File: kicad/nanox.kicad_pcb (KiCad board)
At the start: 4 copper layers, 61.7 x 15.9 mm, 142 parts, among them P1 likely an ESD protection diod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, P2 likely an ESD protection diod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, P3 likely an ESD protection diod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, P4 likely an ESD protection diod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, P5 likely an ESD protection diod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, SW1 push button, left, SW2 push button, right, X1 ?, X10 TI TLV61046A boost converter 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, X11 unknown, marked AF, likely a 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, X12 unknown, likely a P-channel M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, X2 likely an N-channel MOSFET: t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, X3 likely an N-channel MOSFET: t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, X4 ?, X5 ?, X6 ?, X7 ?, X8 ?, X9 NXP PMBZ5246B 16 V Zener diod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, Y1 32 MHz crystal (HSE), Y2 not populated: 32.768 kHz cry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

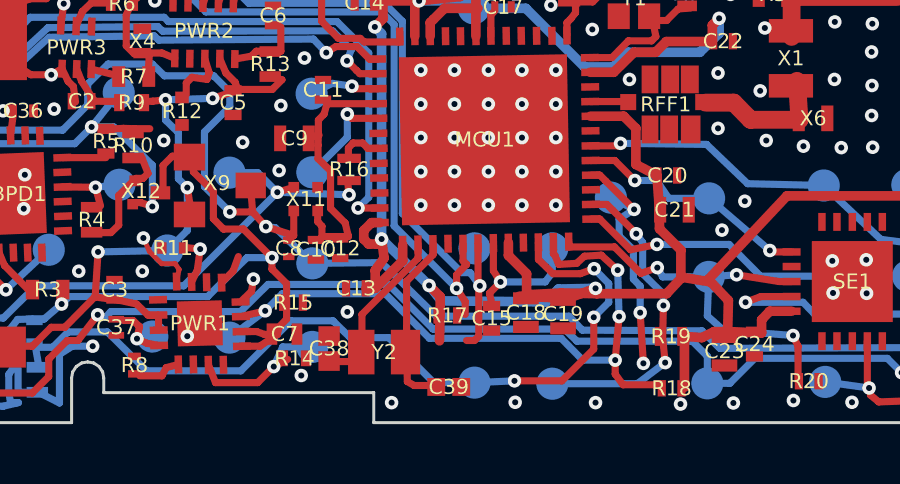
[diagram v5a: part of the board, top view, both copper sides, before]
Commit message: Move R17 onto the I2C1 SCL trace: the clock's pull-up to +3.3V
Co-Authored-By: Claude Opus 5.5 <noreply@anthropic.com>
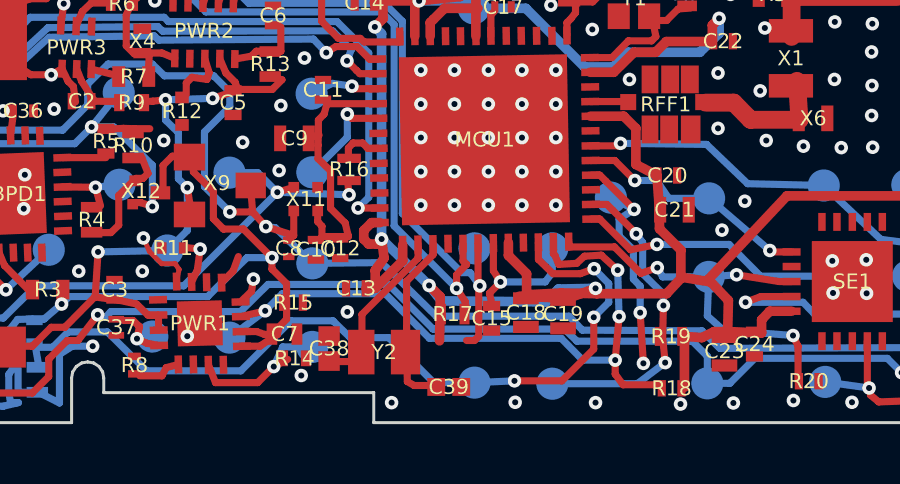
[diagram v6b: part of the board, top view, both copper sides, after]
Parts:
- moved R17 0.18 mm to (28.7, 23.6)
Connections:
- R17 pad 2: (no net) -> I2C1 SCL
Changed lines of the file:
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@@
 	(footprint ""
 		(layer "F.Cu")
+		(at 28.70238 23.571428)
+		(descr "two-terminal SMD")
+		(property "Reference" "R17"
+			(at 0 0 0)
+			(layer "F.SilkS")
+			(effects
+				(font
+					(size 0.5 0.5)
+					(thickness 0.08)
+				)
+			)
+		)
+		(property "Value" "R"
+			(at 0 0 0)
+			(layer "F.Fab")
+			(hide yes)
+			(effects
+				(font
+					(size 1.27 1.27)
+				)
+			)
+		)
+		(property "Datasheet" ""
+			(at 0 0 0)
+			(layer "F.Fab")
+			(hide yes)
+			(effects
+				(font
+					(size 1.27 1.27)
+				)
+			)
+		)
+		(property "Description" ""
+			(at 0 0 0)
+			(layer "F.Fab")
+			(hide yes)
+			(effects
+				(font
+					(size 1.27 1.27)
+				)
+			)
+		)
+		(duplicate_pad_numbers_are_jumpers no)
+		(fp_line
+			(start -0.559523 -0.345238)
+			(end -0.559523 0.345238)
+			(stroke
+				(width 0.08)
+				(type default)
+			)
+			(layer "F.Fab")
+		)
+		(fp_line
+			(start -0.559523 0.345238)
+			(end 0.559524 0.345238)
+			(stroke
+				(width 0.08)
+				(type default)
+			)
+			(layer "F.Fab")
+		)
+		(fp_line
+			(start 0.559524 -0.345238)
+			(end -0.559523 -0.345238)
+			(stroke
+				(width 0.08)
+				(type default)
+			)
+			(layer "F.Fab")
+		)
+		(fp_line
+			(start 0.559524 0.345238)
+			(end 0.559524 -0.345238)
+			(stroke
+				(width 0.08)
+				(type default)
+			)
+			(layer "F.Fab")
+		)
+		(pad "1" smd rect
+			(at -0.392857 0)
+			(size 0.333333 0.690476)
+			(layers "F.Cu" "F.Mask" "F.Paste")
+			(net "+3.3V rail")
+			(thermal_bridge_angle 45)
+		)
+		(pad "2" smd rect
+			(at 0.392858 0)
+			(size 0.333333 0.690476)
+			(layers "F.Cu" "F.Mask" "F.Paste")
+			(net "I2C1 SCL")
+			(thermal_bridge_angle 45)
+		)
+		(embedded_fonts no)
+		(model "/usr/share/kicad/3dmodels/Resistor_SMD.3dshapes/R_0402_1005Metric.step"
+			(offset
+				(xyz 0 0 0)
+			)
+			(scale
+				(xyz 1 1 1)
+			)
+			(rotate
+				(xyz 0 0 0)
+			)
+		)
+	)
+	(footprint ""
+		(layer "F.Cu")
 		(at 40.714285 17.047619)
 		(descr "two-terminal SMD; Two-terminal part in the antenna matching network with a grey/white body; was C27. Either a C0G/NP0 capacitor (often grey or white) or a ceramic chip inductor")
@@
 			)
 		)
-	)
-	(footprint ""
-		(layer "F.Cu")
-		(at 28.523809 23.619047)
-		(descr "two-terminal SMD")
-		(property "Reference" "R17"
-			(at 0 0 0)
-			(layer "F.SilkS")
-			(effects
-				(font
-					(size 0.5 0.5)
-					(thickness 0.08)
-				)
-			)
-		)
-		(property "Value" "R"
-			(at 0 0 0)
-			(layer "F.Fab")
-			(hide yes)
-			(effects
-				(font
-					(size 1.27 1.27)
-				)
-			)
-		)
-		(property "Datasheet" ""
-			(at 0 0 0)
-			(layer "F.Fab")
-			(hide yes)
-			(effects
-				(font
-					(size 1.27 1.27)
-				)
-			)
-		)
-		(property "Description" ""
-			(at 0 0 0)
-			(layer "F.Fab")
-			(hide yes)
-			(effects
-				(font
-					(size 1.27 1.27)
-				)
-			)
-		)
-		(duplicate_pad_numbers_are_jumpers no)
-		(fp_line
-			(start -0.464286 -0.273809)
-			(end -0.464286 0.27381)
-			(stroke
-				(width 0.08)
-				(type default)
-			)
-			(layer "F.Fab")
-		)
-		(fp_line
-			(start -0.464286 0.27381)
-			(end 0.464286 0.27381)
-			(stroke
-				(width 0.08)
-				(type default)
-			)
-			(layer "F.Fab")
-		)
-		(fp_line
-			(start 0.464286 -0.273809)
-			(end -0.464286 -0.273809)
-			(stroke
-				(width 0.08)
-				(type default)
-			)
-			(layer "F.Fab")
-		)
-		(fp_line
-			(start 0.464286 0.27381)
-			(end 0.464286 -0.273809)
-			(stroke
-				(width 0.08)
-				(type default)
-			)
-			(layer "F.Fab")
-		)
-		(pad "1" smd rect
-			(at -0.327381 0)
-			(size 0.273809 0.547619)
-			(layers "F.Cu" "F.Mask" "F.Paste")
-			(net "+3.3V rail")
-			(thermal_bridge_angle 45)
-		)
-		(pad "2" smd rect
-			(at 0.327381 0)
-			(size 0.273809 0.547619)
-			(layers "F.Cu" "F.Mask" "F.Paste")
-			(thermal_bridge_angle 45)
-		)
-		(embedded_fonts no)
-		(model "/usr/share/kicad/3dmodels/Resistor_SMD.3dshapes/R_0402_1005Metric.step"
-			(offset
-				(xyz 0 0 0)
-			)
-			(scale
-				(xyz 1 1 1)
-			)
-			(rotate
-				(xyz 0 0 0)
-			)
-		)

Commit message: Add R36, the I2C1 SDA pull-up next to R17
The automatic pass missed it. It sits between the +3.3V trace and the end
of the SDA trace, which both already ran onto its pads.

Co-Authored-By: Claude Opus 5.5 <noreply@anthropic.com>
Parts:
- added R36: R, , F.Cu at (28.7, 24.5)
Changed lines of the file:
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@@
+	(footprint ""
+		(layer "F.Cu")
+		(at 28.70238 24.45238)
+		(descr "two-terminal SMD; Added by hand: missed by the automatic pass, next to R17")
+		(property "Reference" "R36"
+			(at 0 0 0)
+			(layer "F.SilkS")
+			(effects
+				(font
+					(size 0.5 0.5)
+					(thickness 0.08)
+				)
+			)
+		)
+		(property "Value" "R"
+			(at 0 0 0)
+			(layer "F.Fab")
+			(hide yes)
+			(effects
+				(font
+					(size 1.27 1.27)
+				)
+			)
+		)
+		(property "Datasheet" ""
+			(at 0 0 0)
+			(layer "F.Fab")
+			(hide yes)
+			(effects
+				(font
+					(size 1.27 1.27)
+				)
+			)
+		)
+		(property "Description" ""
+			(at 0 0 0)
+			(layer "F.Fab")
+			(hide yes)
+			(effects
+				(font
+					(size 1.27 1.27)
+				)
+			)
+		)
+		(duplicate_pad_numbers_are_jumpers no)
+		(fp_line
+			(start -0.70238 -0.357142)
+			(end -0.70238 0.357143)
+			(stroke
+				(width 0.08)
+				(type default)
+			)
+			(layer "F.Fab")
+		)
+		(fp_line
+			(start -0.70238 0.357143)
+			(end 0.702381 0.357143)
+			(stroke
+				(width 0.08)
+				(type default)
+			)
+			(layer "F.Fab")
+		)
+		(fp_line
+			(start 0.702381 -0.357142)
+			(end -0.70238 -0.357142)
+			(stroke
+				(width 0.08)
+				(type default)
+			)
+			(layer "F.Fab")
+		)
+		(fp_line
+			(start 0.702381 0.357143)
+			(end 0.702381 -0.357142)
+			(stroke
+				(width 0.08)
+				(type default)
+			)
+			(layer "F.Fab")
+		)
+		(pad "1" smd rect
+			(at -0.494047 0)
+			(size 0.416666 0.714285)
+			(layers "F.Cu" "F.Mask" "F.Paste")
+			(net "+3.3V rail")
+			(thermal_bridge_angle 45)
+		)
+		(pad "2" smd rect
+			(at 0.494048 0)
+			(size 0.416666 0.714285)
+			(layers "F.Cu" "F.Mask" "F.Paste")
+			(net "I2C1 SDA")
+			(thermal_bridge_angle 45)
+		)
+		(embedded_fonts no)
+		(model "/usr/share/kicad/3dmodels/Resistor_SMD.3dshapes/R_0603_1608Metric.step"
+			(offset
+				(xyz 0 0 0)
+			)
+			(scale
+				(xyz 1 1 1)
+			)
+			(rotate
+				(xyz 0 0 0)
+			)
+		)
+	)
 	(footprint ""
 		(layer "F.Cu")

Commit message: Ground USB1's four GND pins (A1, A12, B1, B12) through the pour
Confirmed on the board.

Co-Authored-By: Claude Opus 5.5 <noreply@anthropic.com>
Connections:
- USB1 pad A1: (no net) -> GND
- USB1 pad A12: (no net) -> GND
- USB1 pad B1: (no net) -> GND
- USB1 pad B12: (no net) -> GND
